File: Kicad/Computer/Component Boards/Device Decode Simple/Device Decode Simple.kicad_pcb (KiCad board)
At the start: 2 copper layers, 26.7 x 59.7 mm, 18 parts, among them IC1 AP7365-33WG-7, IC16 74LVC02APW,118, IC2 74LVC138APW-Q100J, IC3 74LVC02APW,118, IC4 74LVC2G04GW-Q100H, IC5 74LVC02APW,118, IC7 SN74F521NSR, IC8 SN74F521NSR, J1 Conn_02x20_Counter_Clockwise

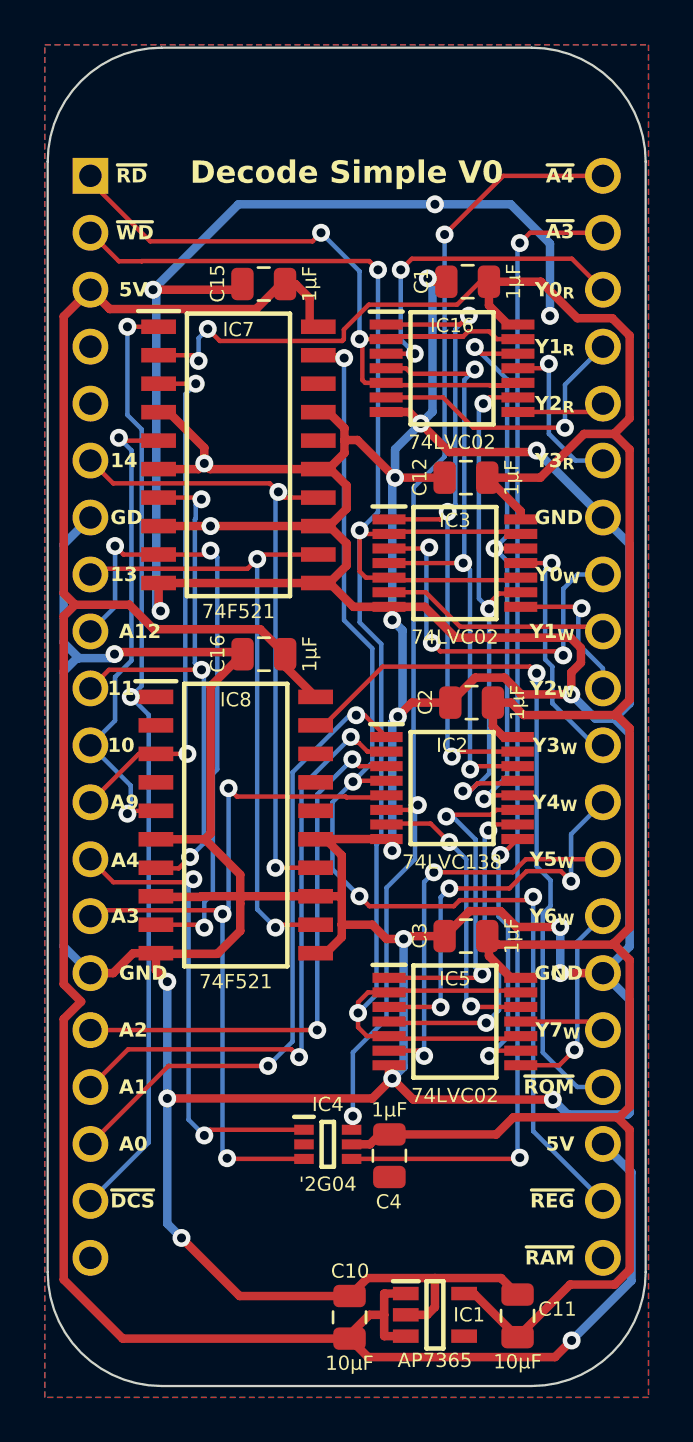
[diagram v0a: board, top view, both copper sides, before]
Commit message: Standardising DIP board layouts.
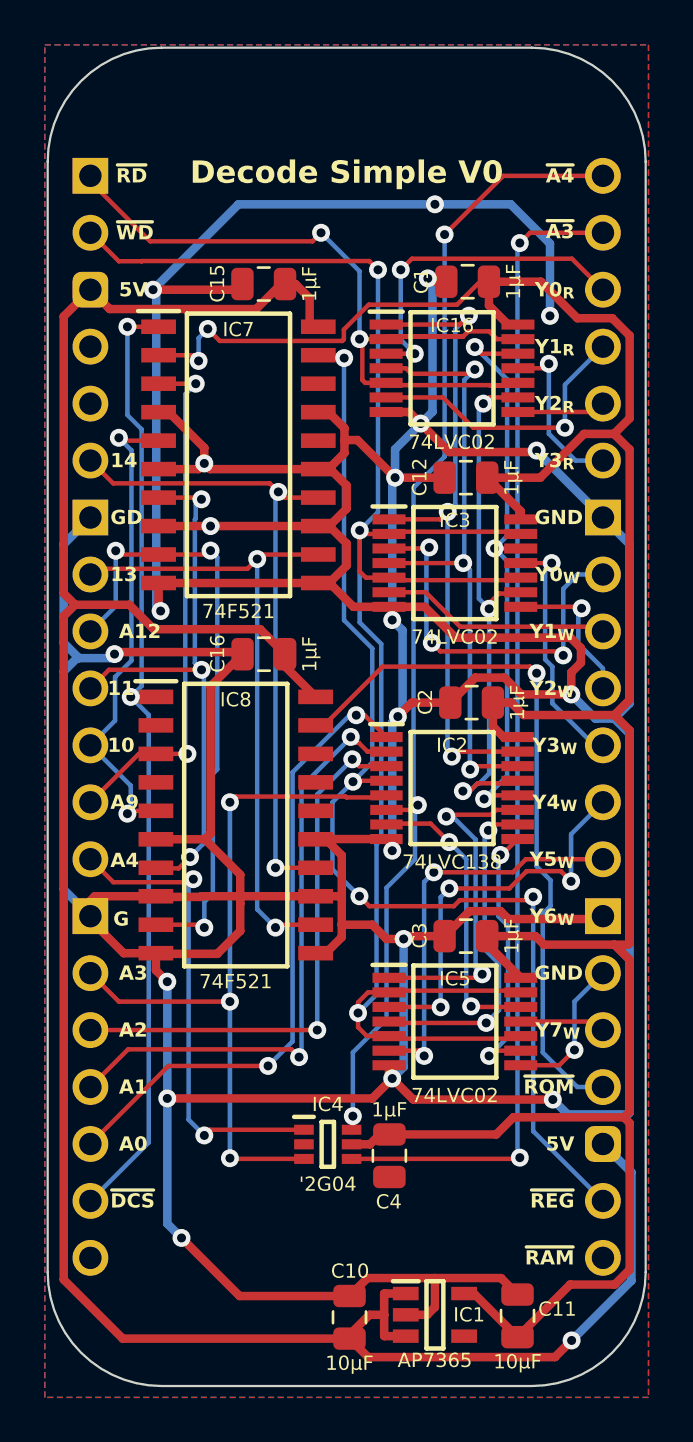
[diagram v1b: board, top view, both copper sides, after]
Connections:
- J1 pad 14: /A3 -> /GND
- J1 pad 15: /GND -> /A3
- J1 pad 26: /GND -> /Y6+W
- J1 pad 27: /Y6+W -> /GND
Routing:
- net /Y6+W: track 9.17 -> 6.63 mm
- net /GND: track 322.6 -> 320.4 mm, vias 23 -> 21
- net /5V: track 110.9 -> 110.3 mm
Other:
- board text added: "G"

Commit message: Added silkscreen to Address Selector.
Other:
- board text removed: "~{RAM}"
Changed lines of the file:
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@@
     (effects (font (size 0.635 0.635) (thickness 0.15) bold) (justify right))
   )
-  (gr_text "A12" (at 90.17 78.74) (layer "F.SilkS")
+  (gr_text "A12" (at 90.1192 78.74) (layer "F.SilkS")
     (effects (font (size 0.635 0.635) (thickness 0.15) bold) (justify left))
   )
@@
     (effects (font (size 0.635 0.635) (thickness 0.15) bold) (justify right))
   )
-  (gr_text "~{RAM}" (at 110.49 106.68) (layer "F.SilkS")
-    (effects (font (size 0.635 0.635) (thickness 0.15) bold) (justify right))
-  )

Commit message: Resized 15mm wide boards and fixed GND pins.  Added GPIO 4bit and PS2 Board.
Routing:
- net /GND: track 320.4 -> 325.8 mm, vias 21 -> 22
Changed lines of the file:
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@@
   (via (at 110.347043 81.549957) (size 0.8) (drill 0.4) (layers "F.Cu" "B.Cu") (net 2))
   (via (at 102.489 71.882) (size 0.8) (drill 0.4) (layers "F.Cu" "B.Cu") (net 2))
+  (via (at 92.964 111.1504) (size 0.8) (drill 0.4) (layers "F.Cu" "B.Cu") (net 2))
   (segment (start 111.76 73.66) (end 112.95 74.85) (width 0.38) (layer "B.Cu") (net 2))
   (segment (start 87.71 90.25) (end 88.9 91.44) (width 0.38) (layer "B.Cu") (net 2))
@@
   (segment (start 92.329 99.568) (end 92.329 94.361002) (width 0.38) (layer "B.Cu") (net 2))
   (segment (start 92.329 99.568) (end 92.329 105.155992) (width 0.38) (layer "B.Cu") (net 2))
+  (segment (start 92.964003 105.790995) (end 92.964 105.790998) (width 0.38) (layer "B.Cu") (net 2))
   (segment (start 87.71 79.248) (end 88.392 79.93) (width 0.38) (layer "B.Cu") (net 2))
   (segment (start 89.797711 79.93) (end 89.976138 79.751573) (width 0.38) (layer "B.Cu") (net 2))
@@
   (segment (start 88.298 79.93) (end 87.71 80.518) (width 0.38) (layer "B.Cu") (net 2))
   (segment (start 102.489 70.612) (end 103.632 69.469) (width 0.38) (layer "B.Cu") (net 2))
+  (segment (start 92.964 105.790998) (end 92.964 111.1504) (width 0.38) (layer "B.Cu") (net 2))
   (segment (start 104.158 68.943) (end 104.158 63.204715) (width 0.38) (layer "B.Cu") (net 2))
   (segment (start 112.877599 100.2792) (end 110.1852 100.2792) (width 0.38) (layer "B.Cu") (net 2))

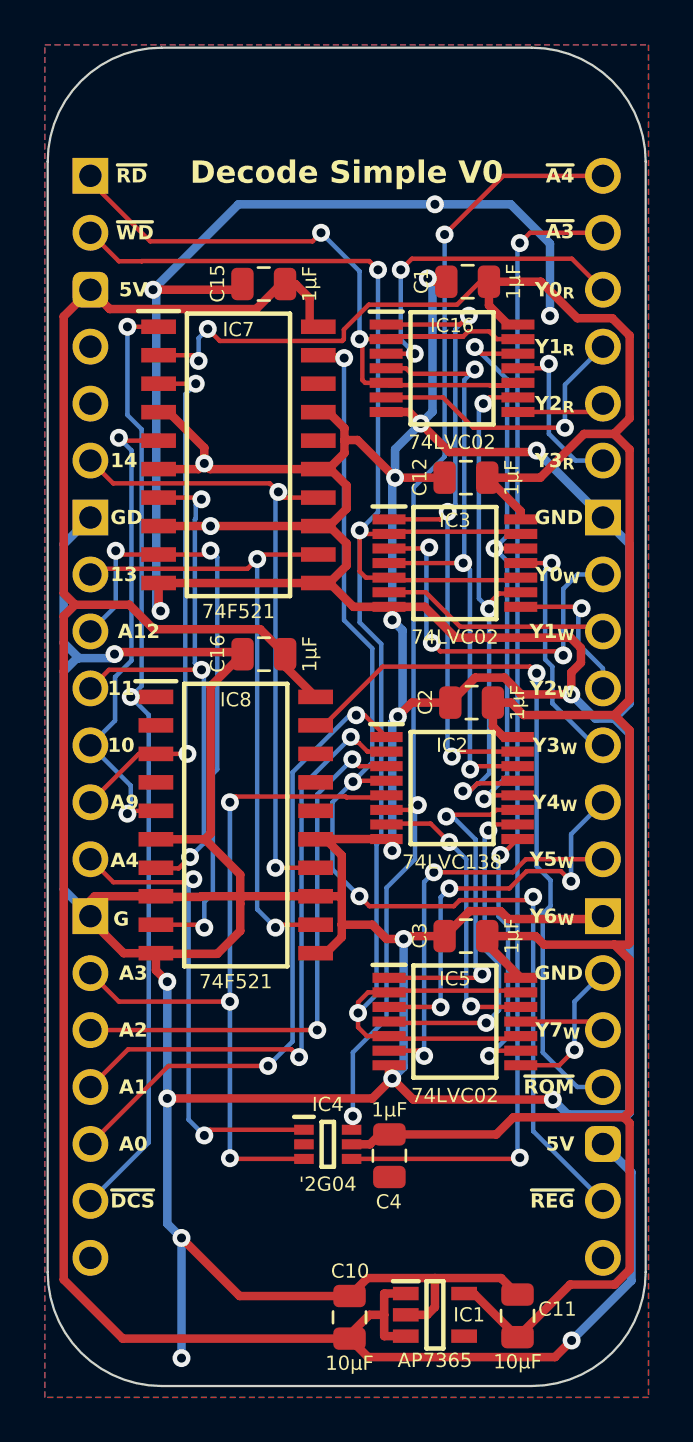
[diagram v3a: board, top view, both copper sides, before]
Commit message: Added State Reader and re-routed Device Decode stage B.
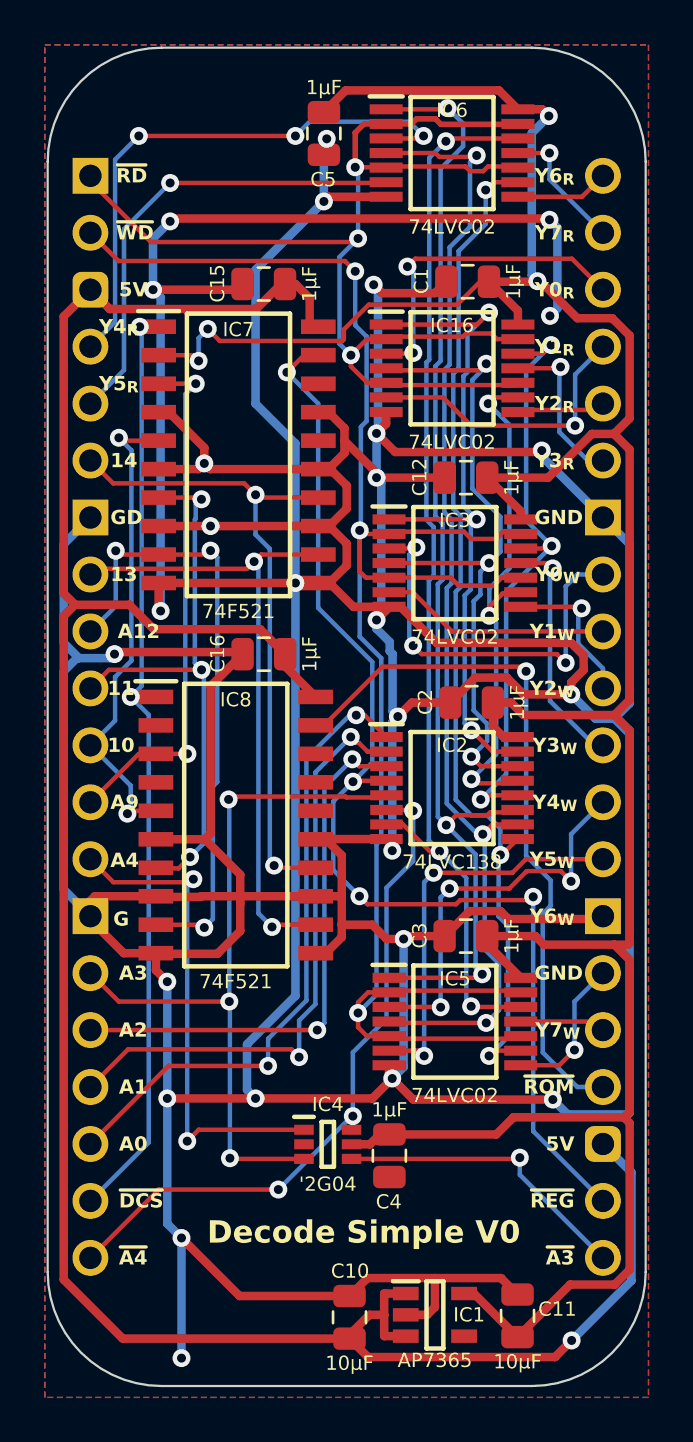
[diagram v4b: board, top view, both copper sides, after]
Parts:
- added C5: 1μF, SamacSys_Parts:C_0805, F.Cu at (99.3, 56.5)
- added IC6: 74LVC02APW,118, SamacSys_Parts:SOP65P640X110-14N, F.Cu at (105.0, 57.4)
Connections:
- J1 pad 20: unconnected-(J1-Pin_20-Pad20) -> /~{A4}
- J1 pad 21: unconnected-(J1-Pin_21-Pad21) -> /~{A3}
- J1 pad 39: /~{A3} -> /Y7+R
- J1 pad 4: unconnected-(J1-Pin_4-Pad4) -> /Y4+R
- J1 pad 40: /~{A4} -> /Y6+R
- J1 pad 5: unconnected-(J1-Pin_5-Pad5) -> /Y5+R
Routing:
- net /GND: track 325.8 -> 380.2 mm, vias 22 -> 27
- net /~{A3}: track 52.3 -> 13.5 mm, vias 2 -> 1
- net /~{Y5}: track 14.8 -> 51.0 mm, vias 2 -> 3
- net /~{Y4}: track 15.4 -> 50.8 mm, vias 2 -> 3
- net /~{Y7}: track 13.1 -> 48.3 mm, vias 2 -> 3
- net /~{Y6}: track 11.9 -> 45.2 mm, vias 2 -> 3
- net /Y4+R: track 0.00 -> 25.2 mm, vias 0 -> 3
- net /Y5+R: track 0.00 -> 20.9 mm, vias 0 -> 1
- net /~{A4}: track 51.4 -> 30.9 mm
- net /3.3V: track 116.7 -> 135.6 mm, vias 2 -> 4
- net /~{RD}: track 37.3 -> 54.4 mm, vias 2 -> 3
- net /Y7+R: track 0.00 -> 5.95 mm, vias 0 -> 1
- net /Y6+R: track 0.00 -> 4.18 mm
- net /~{Y1}: track 27.8 -> 30.5 mm
- net /~{Y0}: track 29.8 -> 30.9 mm
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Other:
- board text added: "Y4_{R}"
- board text added: "Y5_{R}"
- board text added: "Y6_{R}"
- board text added: "Y7_{R}"
